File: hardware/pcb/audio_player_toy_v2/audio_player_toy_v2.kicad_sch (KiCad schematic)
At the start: 19 parts, among them J1 Conn_02x05_Odd_Even, U1 ISD2360YYI, U2 BH-AAA-B5AA005

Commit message: feat: finish schematics of v2
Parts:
- removed C1: EEEFK1A221V, .pretty:CAP_EEEFK1A221V, symbol EEEFK1A221V:EEEFK1A221V
- removed C3: 4.7uF, Capacitor_SMD:C_0603_1608Metric, symbol Device:C
- removed D1: 1N5817WS_C727114, .pretty:SOD-323_L1.8-W1.3-LS2.5-FD, symbol .kicad_sym:1N5817WS_C727114
- removed U2: BH-AAA-B5AA005, .pretty:BAT-SMD_BH-AAA-B5AA005, symbol .kicad_sym:BH-AAA-B5AA005
- added C1, C4: 47uF, symbol Device:C_Polarized
- added C5: 0.1uF, Resistor_SMD:R_0603_1608Metric, symbol Device:C
- added FL1: BLM18PG601SN1, BLM18EG601SN1D:BEADC1608X95N, symbol BLM18EG601SN1D:BLM18EG601SN1D
- added J2: USB_C_Receptacle_USB2.0_14P, symbol Connector:USB_C_Receptacle_USB2.0_14P
- added R4: 5.1K, Resistor_SMD:R_0603_1608Metric, symbol Device:R
- added R5: 5.1K, symbol Device:R
- C2: value 4.7uF -> 10uF; footprint Capacitor_SMD:C_0603_1608Metric -> Resistor_SMD:R_0603_1608Metric; Component GRM188Z71C475KE21D -> (none); Detail +-10%, 16V -> (none)
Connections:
- net GND: now also C1.2, C4.2, C5.2, J2.A1 (GND), J2.A12 (GND), J2.B1 (GND), J2.B12 (GND), J2.S1 (SHIELD), R4.2, R5.2
- net BAT+ renamed VCC
- net VCC: now also C1.1, C4.1, C5.1, FL1.2
- new net: J2.B5 (CC2), R4.1
- new net: J2.A5 (CC1), R5.1
- new net USB_VBUS: FL1.1, J2.A4 (VBUS), J2.A9 (VBUS), J2.B4 (VBUS), J2.B9 (VBUS)
- no-connect marks 18 -> 22
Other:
- moved on the sheet: H1, H2, H3, H4, R1, R2, R3, S1, S2, S3, U1

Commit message: chore: complete finding all footprints, ready to routing, both version
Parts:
- removed C4: 47uF, symbol Device:C_Polarized
- removed J2: USB_C_Receptacle_USB2.0_14P, symbol Connector:USB_C_Receptacle_USB2.0_14P
- added C2: 47uF, .pretty:CASE-A_3216, symbol Device:C_Polarized
- added J3: TYPE-C-31-M-12, TYPE-C-31-M-12:HRO_TYPE-C-31-M-12, symbol TYPE-C-31-M-12:TYPE-C-31-M-12
- C1: footprint (none) -> .pretty:CASE-A_3216; Component (none) -> TLJA476M010R0600; Detail (none) -> +-20%, 10V, 600mΩ; Manufactor (none) -> KYOCERA AVX
- FL1: footprint BLM18EG601SN1D:BEADC1608X95N -> .pretty:BEADC1608X95N
- R5: footprint (none) -> Resistor_SMD:R_0603_1608Metric
- renumbered C5 to C3, C2 to C4
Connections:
- net GND: now also C2.2, J3.A1_B12 (GND), J3.B1_A12 (GND), J3.S1 (SHIELD), J3.S2 (SHIELD), J3.S3 (SHIELD), J3.S4 (SHIELD)
- net VCC: now also C2.1
- net at R4.1: now also J3.B5 (CC2)
- net at R5.1: now also J3.A5 (CC1)
- net USB_VBUS renamed VBUS
- net VBUS: now also J3.A4_B9 (VBUS), J3.B4_A9 (VBUS)
- no-connect marks 22 -> 24
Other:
- moved on the sheet: R4, R5

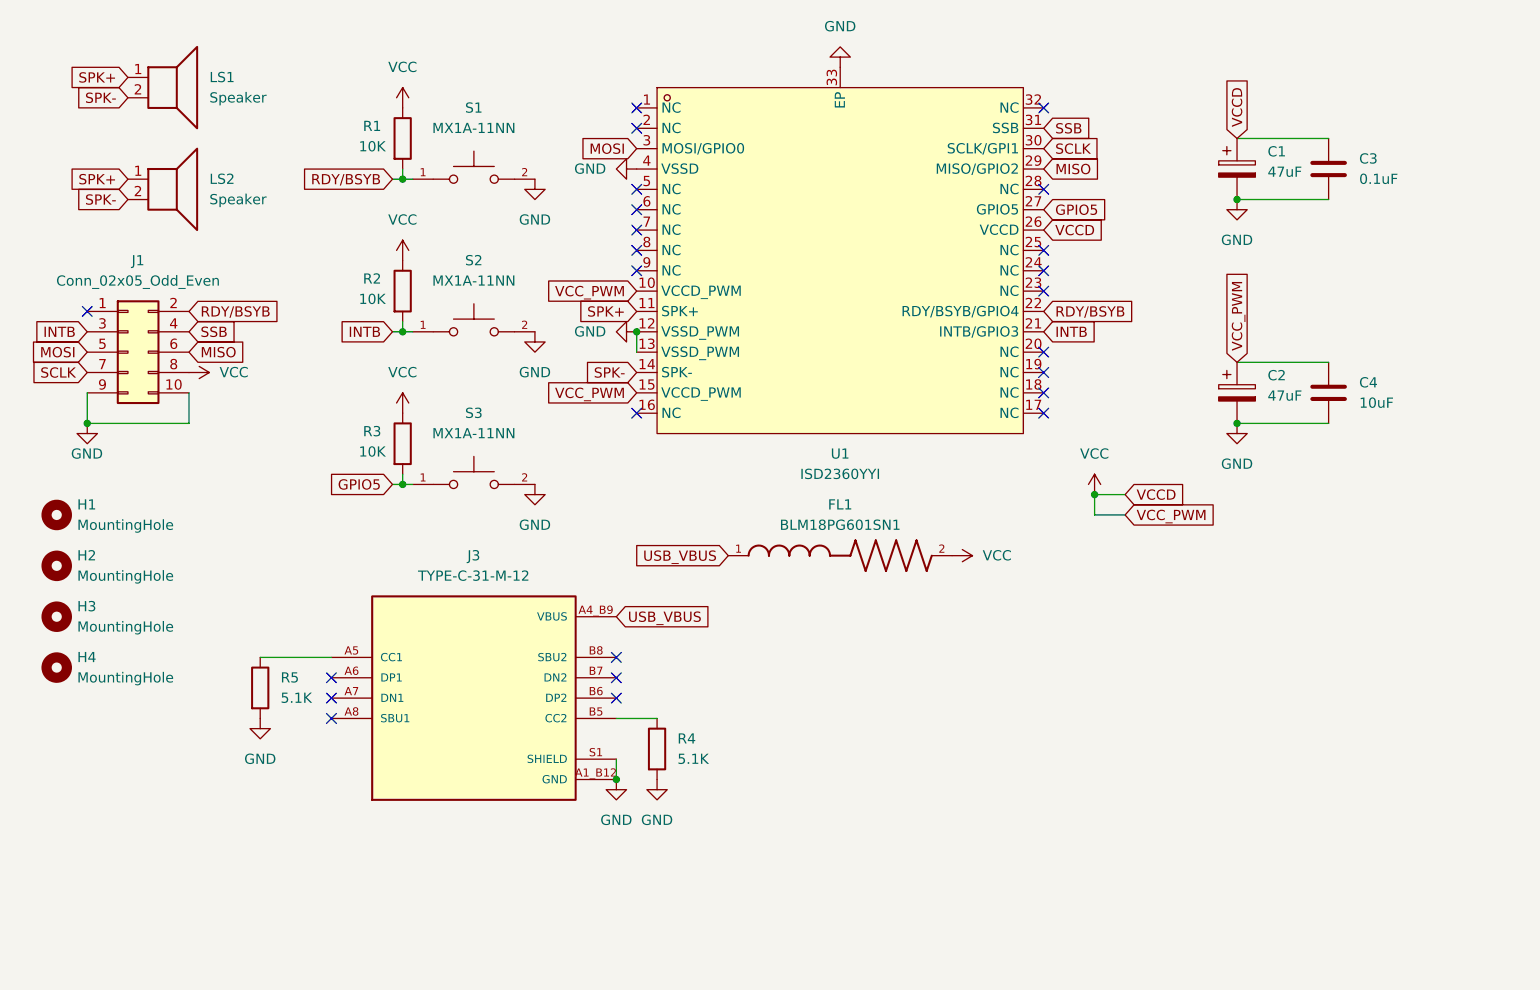
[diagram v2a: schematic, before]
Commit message: chore: update decoupling caps in v1
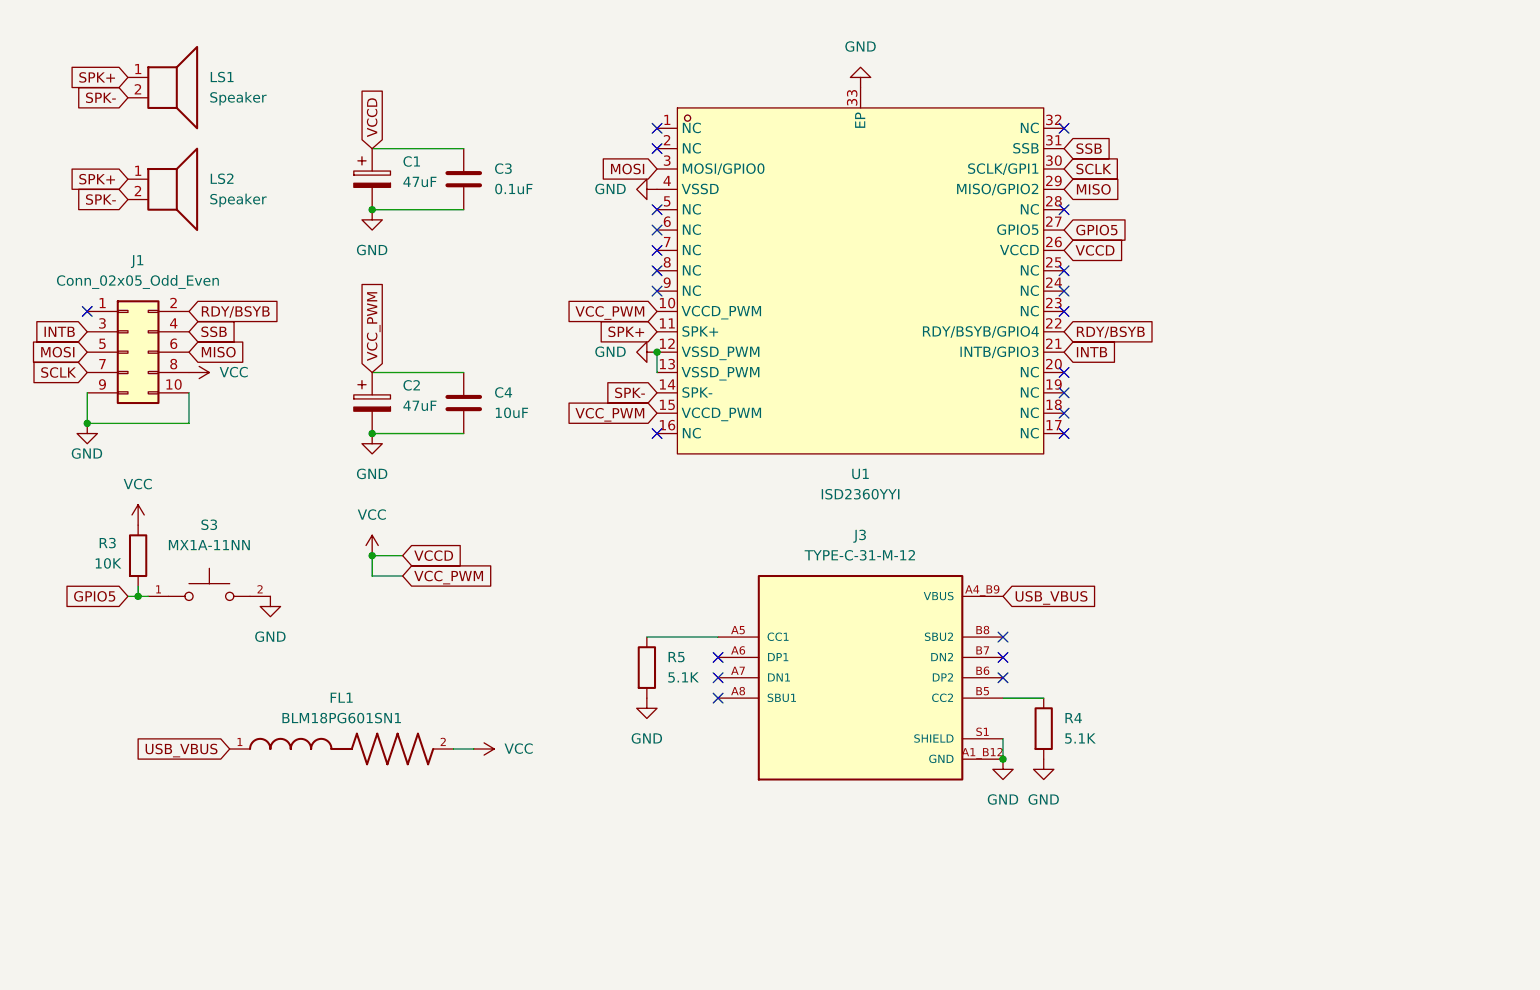
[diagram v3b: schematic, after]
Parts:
- removed H1, H2, H3, H4: MountingHole, MountingHole:MountingHole_3.2mm_M3, symbol Mechanical:MountingHole
- removed R1, R2: 10K, Resistor_SMD:R_0603_1608Metric, symbol Device:R
- removed S1, S2: MX1A-11NN, .pretty:SW_MX1A-11NN, symbol MX1A-11NN:MX1A-11NN
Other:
- moved on the sheet: C1, C2, C3, C4, FL1, J3, R3, R4, R5, S3, U1

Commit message: feat: finish routing v2
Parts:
- removed C1, C2: 47uF, .pretty:CASE-A_3216, symbol Device:C_Polarized
- added C2: TAJA226M010RNJ, .pretty:CAPMP3216X180N, symbol TAJA226M010RNJ:TAJA226M010RNJ
- J2: renamed from J3; footprint TYPE-C-31-M-12:HRO_TYPE-C-31-M-12 -> .pretty:HRO_TYPE-C-31-M-12
- renumbered C4 to C1, R3 to R1, R5 to R2, R4 to R3, S3 to S1
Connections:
- net GND: now also C2.2
- net VCC: now also C2.1
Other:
- moved on the sheet: C1, FL1, J1, LS1, LS2, R1, S1

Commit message: doc: generate BOM for v1 and v2
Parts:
- C1: Component (none) -> GRM188R61C106KAALD; Detail (none) -> +-10%, 16V, X5R; Manufactor (none) -> MuRata
- C3: Component (none) -> GCJ188R71C104KA01D; Detail (none) -> +-10%, 16V, X7R; Manufactor (none) -> MuRata
- R1: Component (none) -> RC0603FR-0710KL; Detail (none) -> +-1%, 100mW; Manufactor (none) -> Yageo
- R2, R3: Component (none) -> RC0603FR-075K1L; Detail (none) -> +-1%, 100mW; Manufactor (none) -> Yageo
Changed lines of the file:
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@@
 			)
 		)
-		(property "Manufactor" ""
+		(property "Manufactor" "Yageo"
+			(at 142.24 102.87 0)
+			(effects
+				(font
+					(size 1.27 1.27)
+				)
+				(hide yes)
+			)
+		)
+		(property "Component" "RC0603FR-075K1L"
+			(at 142.24 102.87 0)
+			(effects
+				(font
+					(size 1.27 1.27)
+				)
+				(hide yes)
+			)
+		)
+		(property "Detail" "+-1%, 100mW"
 			(at 142.24 102.87 0)
 			(effects
@@
 			)
 		)
-		(property "Manufactor" ""
+		(property "Manufactor" "MuRata"
+			(at 69.85 34.29 0)
+			(effects
+				(font
+					(size 1.27 1.27)
+				)
+				(hide yes)
+			)
+		)
+		(property "Component" "GCJ188R71C104KA01D"
+			(at 69.85 34.29 0)
+			(effects
+				(font
+					(size 1.27 1.27)
+				)
+				(hide yes)
+			)
+		)
+		(property "Detail" "+-10%, 16V, X7R"
 			(at 69.85 34.29 0)
 			(effects
@@
 			)
 		)
-		(property "Manufactor" ""
+		(property "Manufactor" "MuRata"
+			(at 55.88 34.29 0)
+			(effects
+				(font
+					(size 1.27 1.27)
+				)
+				(hide yes)
+			)
+		)
+		(property "Component" "    GRM188R61C106KAALD"
+			(at 55.88 34.29 0)
+			(effects
+				(font
+					(size 1.27 1.27)
+				)
+				(hide yes)
+			)
+		)
+		(property "Detail" "+-10%, 16V, X5R"
 			(at 55.88 34.29 0)
 			(effects
@@
 			)
 		)
-		(property "Manufactor" ""
+		(property "Manufactor" "Yageo"
+			(at 92.71 95.25 0)
+			(effects
+				(font
+					(size 1.27 1.27)
+				)
+				(hide yes)
+			)
+		)
+		(property "Component" "RC0603FR-075K1L"
+			(at 92.71 95.25 0)
+			(effects
+				(font
+					(size 1.27 1.27)
+				)
+				(hide yes)
+			)
+		)
+		(property "Detail" "+-1%, 100mW"
 			(at 92.71 95.25 0)
 			(effects
@@
 			)
 		)
-		(property "Manufactor" ""
+		(property "Manufactor" "Yageo"
 			(at 59.69 72.39 0)
 			(effects
+				(font
+					(size 1.27 1.27)
+				)
+				(hide yes)
+			)
+		)
+		(property "Component" "RC0603FR-0710KL"
+			(at 59.69 72.39 0)
+			(effects
+				(font
+					(size 1.27 1.27)
+				)
+				(hide yes)
+			)
+		)
+		(property "Detail" "+-1%, 100mW"
+			(at 59.69 72.39 0)
+			(effects

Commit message: doc: generate production data of v1 and v2
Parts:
- C1: Component GRM188R61C106KAALD -> GRM188R61C106KAALD
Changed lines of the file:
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@@
 			)
 		)
-		(property "Component" "    GRM188R61C106KAALD"
+		(property "Component" "GRM188R61C106KAALD"
 			(at 55.88 34.29 0)
 			(effects
